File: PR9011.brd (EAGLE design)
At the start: 148 x 100 mm, 65 parts, among them J1 M3_SCREW_POST, SW1 SPST_TACT-KMR2, Y1 32.768kHz

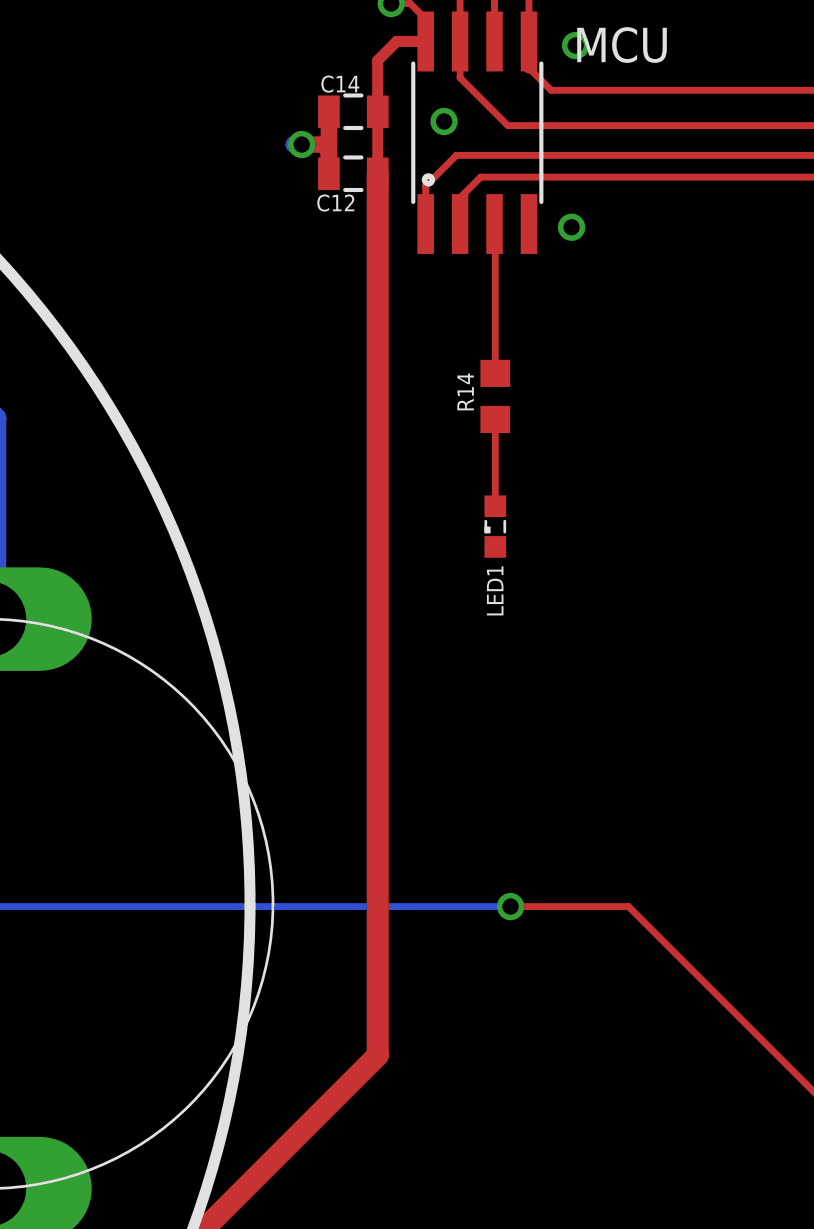
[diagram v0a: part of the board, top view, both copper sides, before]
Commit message: Updated SCH
Updated Pullup Resist & Decoupling Vals
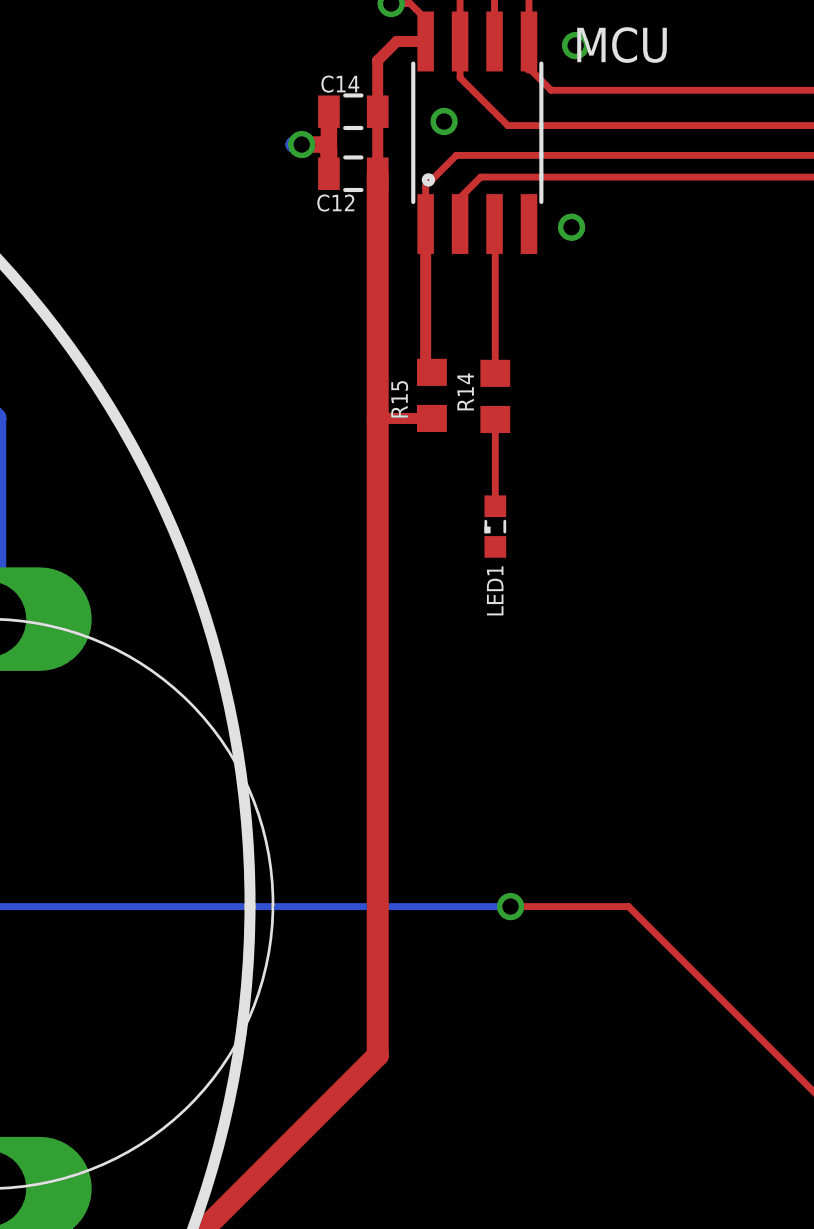
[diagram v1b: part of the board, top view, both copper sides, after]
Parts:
- added R15: 10K, resistor:R0603
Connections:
- net PB5: now also R15.2
- net VCC: now also R15.1
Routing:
- net PB5: track 23.7 -> 29.4 mm
- net VCC: track 183.8 -> 185.8 mm
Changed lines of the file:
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@@
 </element>
 <element name="VARI" library="coilcraft-trimmer" package="146/150" value="" x="34.7" y="31.85" smashed="yes" rot="R180"/>
+<element name="R15" library="resistor" package="R0603" value="10K" x="115.1" y="56.85" smashed="yes" rot="R90">
+<attribute name="NAME" x="114.211" y="55.961" size="0.6096" layer="25" rot="R90"/>
+<attribute name="VALUE" x="117.132" y="55.961" size="1.27" layer="27" rot="R90"/>
+</element>
 </elements>
 <signals>
@@
 <wire x1="99.082" y1="18.49" x2="92.452" y2="18.49" width="0.8128" layer="1"/>
 <wire x1="100.736" y1="20.144" x2="113.102" y2="32.51" width="0.8128" layer="1"/>
-<wire x1="113.102" y1="32.51" x2="113.102" y2="65.024" width="0.8128" layer="1"/>
+<wire x1="113.102" y1="32.51" x2="113.102" y2="56" width="0.8128" layer="1"/>
+<wire x1="113.102" y1="56" x2="113.102" y2="65.024" width="0.8128" layer="1"/>
 <wire x1="114.869" y1="69.9008" x2="114.8682" y2="69.9" width="0.254" layer="1"/>
 <wire x1="113.102" y1="67.31" x2="113.1" y2="67.312" width="0.4064" layer="1"/>
@@
 <wire x1="78.75" y1="14.75" x2="82.49" y2="18.49" width="0.6096" layer="1"/>
 <wire x1="82.49" y1="18.49" x2="92.452" y2="18.49" width="0.6096" layer="1"/>
+<contactref element="R15" pad="1"/>
+<wire x1="115.1" y1="56" x2="113.102" y2="56" width="0.4064" layer="1"/>
 </signal>
 <signal name="N$4">
@@
 <wire x1="116" y1="65.7" x2="134.64" y2="65.7" width="0.254" layer="1"/>
 <wire x1="134.64" y1="65.7" x2="136.078" y2="64.262" width="0.254" layer="1"/>
+<contactref element="R15" pad="2"/>
+<wire x1="115.1" y1="57.7" x2="114.869" y2="57.7" width="0.4064" layer="1"/>
+<wire x1="114.869" y1="57.7" x2="114.869" y2="63.1698" width="0.4064" layer="1"/>
 </signal>
 <signal name="PB1">

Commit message: Updated SCH
Updated SCH
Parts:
- C10: value 1.0uF -> 22nF
- C11: value 1.0uF -> 4.7uF
- C8: value 1.0uF -> .1uF
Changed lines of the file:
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@@
 <?xml version="1.0" encoding="utf-8"?>
 <!DOCTYPE eagle SYSTEM "eagle.dtd">
-<eagle version="6.6.0">
+<eagle version="7.2.0">
 <drawing>
 <settings>
@@
 <layer number="56" name="wert" color="7" fill="1" visible="no" active="no"/>
 <layer number="57" name="tCAD" color="7" fill="1" visible="no" active="no"/>
-<layer number="90" name="Modules" color="5" fill="1" visible="yes" active="yes"/>
+<layer number="90" name="Modules" color="5" fill="1" visible="no" active="no"/>
 <layer number="91" name="Nets" color="2" fill="1" visible="no" active="no"/>
 <layer number="92" name="Busses" color="1" fill="1" visible="no" active="no"/>
@@
 <pass name="Default">
 <param name="RoutingGrid" value="50mil"/>
+<param name="AutoGrid" value="1"/>
+<param name="Efforts" value="0"/>
+<param name="TopRouterVariant" value="1"/>
 <param name="tpViaShape" value="round"/>
 <param name="PrefDir.1" value="|"/>
@@
 <attribute name="VALUE" x="33.919" y="38.876" size="0.4064" layer="27" rot="R270"/>
 </element>
-<element name="C8" library="SparkFun-Capacitors" package="0805" value="1.0uF" x="21.136" y="42.21" smashed="yes" rot="R180">
+<element name="C8" library="SparkFun-Capacitors" package="0805" value=".1uF" x="21.136" y="42.21" smashed="yes" rot="R180">
 <attribute name="PROD_ID" value="CAP-11625" x="5.896" y="123.49" size="1.778" layer="27" rot="R180" display="off"/>
 <attribute name="NAME" x="17.2845" y="42.452" size="0.6096" layer="25" rot="R180"/>
 <attribute name="VALUE" x="22.152" y="43.607" size="0.4064" layer="27" rot="R180"/>
 </element>
-<element name="C10" library="SparkFun-Capacitors" package="0805" value="1.0uF" x="20.986" y="31.768" smashed="yes" rot="R180">
+<element name="C10" library="SparkFun-Capacitors" package="0805" value="22nF" x="20.986" y="31.768" smashed="yes" rot="R180">
 <attribute name="PROD_ID" value="CAP-11625" x="-36.164" y="109.238" size="1.778" layer="27" rot="R180" display="off"/>
 <attribute name="NAME" x="17.6925" y="31.802" size="0.6096" layer="25" rot="R180"/>
 <attribute name="VALUE" x="22.002" y="33.165" size="0.4064" layer="27" rot="R180"/>
 </element>
-<element name="C11" library="SparkFun-Capacitors" package="0805" value="1.0uF" x="20.986" y="29.544" smashed="yes" rot="R180">
+<element name="C11" library="SparkFun-Capacitors" package="0805" value="4.7uF" x="20.986" y="29.544" smashed="yes" rot="R180">
 <attribute name="PROD_ID" value="CAP-11625" x="-39.974" y="107.014" size="1.778" layer="27" rot="R180" display="off"/>
 <attribute name="NAME" x="17.5685" y="29.752" size="0.6096" layer="25" rot="R180"/>

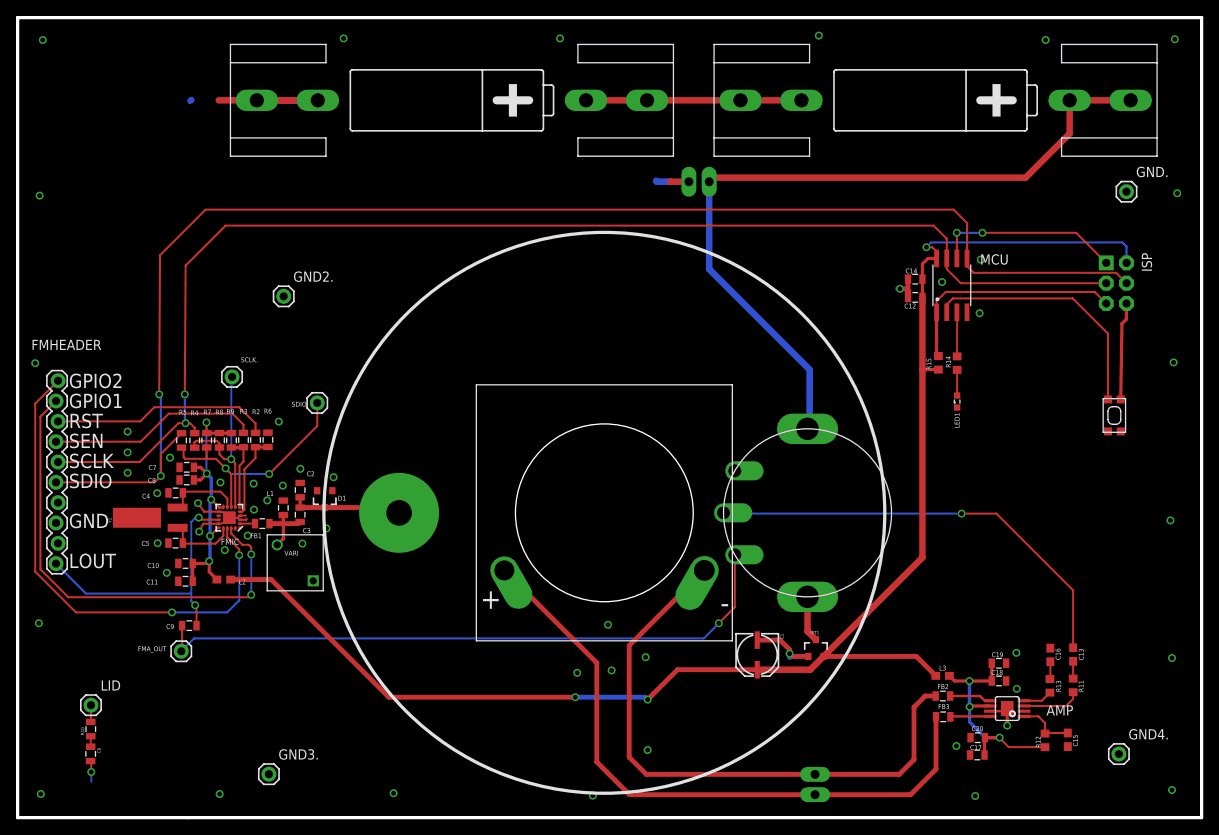
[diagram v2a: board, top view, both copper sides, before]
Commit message: Updated SCH
Updated SCH
JST
Fiducials
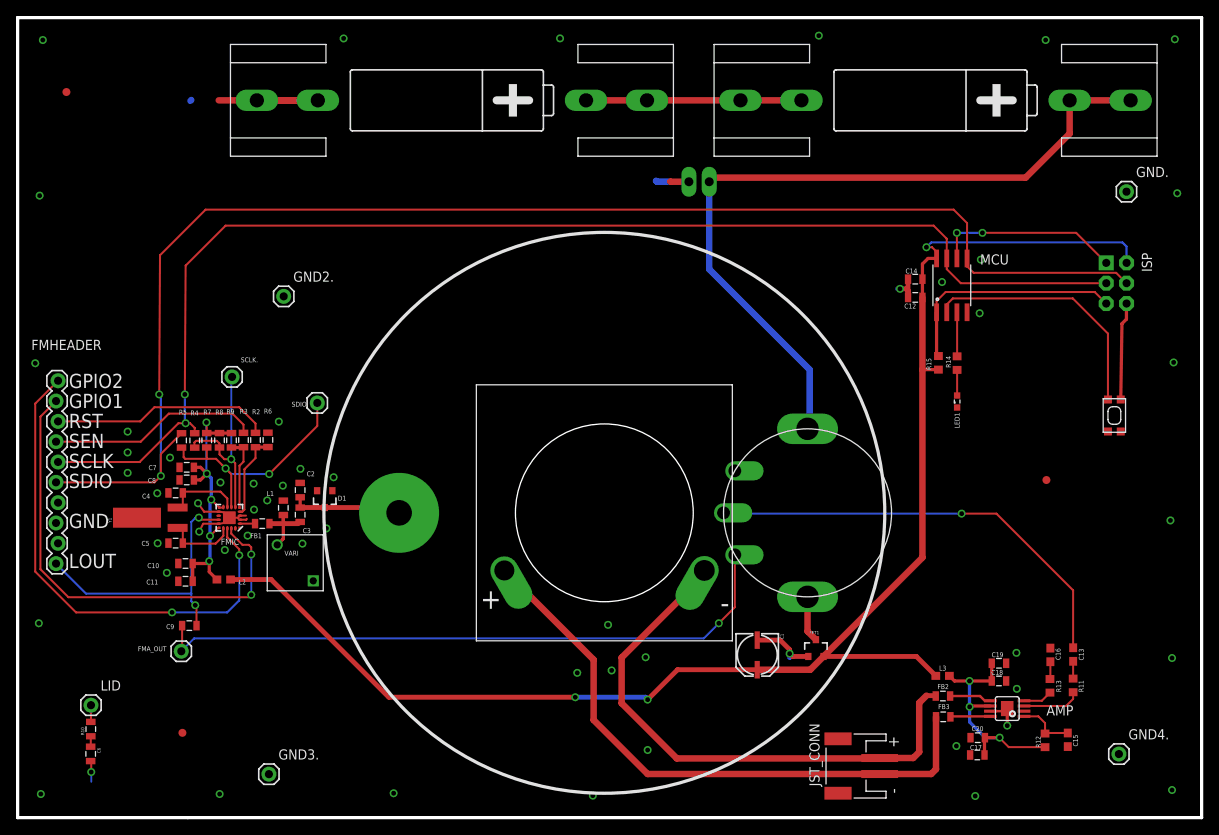
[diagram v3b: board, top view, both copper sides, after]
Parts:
- removed SPK: M02PTH3, SparkFun-Connectors:1X02_LONGPADS
- added JST_CONN: (no value), adafruit:JST-PH-2-SMT-RA
- added U$1, U$2, U$4: FIDUCIAL, adafruit:FIDUCIAL_1MM
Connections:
- net N$9: now also JST_CONN.1; no longer SPK.1
- net OUT-: now also JST_CONN.2; no longer SPK.2
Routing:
- net OUT-: track 80.7 -> 75.7 mm
- net N$9: track 74.3 -> 70.4 mm
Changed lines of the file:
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@@
 <?xml version="1.0" encoding="utf-8"?>
 <!DOCTYPE eagle SYSTEM "eagle.dtd">
-<eagle version="7.2.0">
+<eagle version="6.6.0">
 <drawing>
 <settings>
@@
 <setting verticaltext="up"/>
 </settings>
-<grid distance="0.05" unitdist="mm" unit="mm" style="lines" multiple="1" display="yes" altdistance="0.025" altunitdist="inch" altunit="inch"/>
+<grid distance="0.1" unitdist="mm" unit="mm" style="lines" multiple="1" display="yes" altdistance="0.025" altunitdist="inch" altunit="inch"/>
 <layers>
 <layer number="1" name="Top" color="4" fill="1" visible="yes" active="yes"/>
@@
 <pass name="Default">
 <param name="RoutingGrid" value="50mil"/>
-<param name="AutoGrid" value="1"/>
-<param name="Efforts" value="0"/>
-<param name="TopRouterVariant" value="1"/>
 <param name="tpViaShape" value="round"/>
 <param name="PrefDir.1" value="|"/>
@@
 </element>
 <element name="SW1" library="adafruit" package="KMR2" value="SPST_TACT-KMR2" x="137.092" y="50.266" smashed="yes" rot="R90"/>
-<element name="SPK" library="SparkFun-Connectors" package="1X02_LONGPADS" value="M02PTH3" x="99.684" y="5.408" rot="R270"/>
 <element name="ISP" library="SparkFun-Connectors" package="2X3-NS" value="AVR_SPI_PRG_6NS" x="137.348" y="66.802" locked="yes" smashed="yes" rot="R270">
 <attribute name="NAME" x="140.523" y="70.612" size="1.27" layer="25" ratio="10" rot="R270"/>
@@
 <attribute name="VALUE" x="117.132" y="55.961" size="1.27" layer="27" rot="R90"/>
 </element>
+<element name="JST_CONN" library="adafruit" package="JST-PH-2-SMT-RA" value="" x="104.05" y="6.45" rot="R90"/>
+<element name="U$1" library="adafruit" package="FIDUCIAL_1MM" value="FIDUCIAL" x="128.6" y="42.2"/>
+<element name="U$2" library="adafruit" package="FIDUCIAL_1MM" value="FIDUCIAL" x="6.1" y="90.7"/>
+<element name="U$4" library="adafruit" package="FIDUCIAL_1MM" value="FIDUCIAL" x="20.6" y="10.6"/>
 </elements>
 <signals>
@@
 </signal>
 <signal name="OUT-">
-<contactref element="SPK" pad="2"/>
 <contactref element="U$3" pad="+"/>
 <contactref element="FB3" pad="1"/>
-<wire x1="114.8" y1="12.6" x2="114.8" y2="6.05" width="0.6096" layer="1"/>
-<wire x1="114.8" y1="6.05" x2="111.618" y2="2.868" width="0.6096" layer="1"/>
-<wire x1="111.618" y1="2.868" x2="99.684" y2="2.868" width="0.6096" layer="1"/>
-<wire x1="99.684" y1="2.868" x2="76.482" y2="2.868" width="0.6096" layer="1"/>
-<wire x1="76.482" y1="2.868" x2="72.4" y2="6.95" width="0.6096" layer="1"/>
-<wire x1="72.4" y1="6.95" x2="72.4" y2="19.34" width="0.6096" layer="1"/>
-<wire x1="72.4" y1="19.34" x2="60.84" y2="30.9" width="0.6096" layer="1"/>
+<wire x1="114.8" y1="12.6" x2="114.8" y2="6.05" width="0.8128" layer="1"/>
+<contactref element="JST_CONN" pad="2"/>
+<wire x1="114.8" y1="6.05" x2="114.2" y2="5.45" width="0.8128" layer="1"/>
+<wire x1="114.2" y1="5.45" x2="107.75" y2="5.45" width="0.8128" layer="1"/>
+<wire x1="107.75" y1="5.45" x2="78.75" y2="5.45" width="0.8128" layer="1"/>
+<wire x1="78.75" y1="5.45" x2="72" y2="12.2" width="0.8128" layer="1"/>
+<wire x1="72" y1="12.2" x2="72" y2="19.74" width="0.8128" layer="1"/>
+<wire x1="72" y1="19.74" x2="60.84" y2="30.9" width="0.8128" layer="1"/>
 </signal>
 <signal name="N$34">
@@
 </signal>
 <signal name="N$9">
-<contactref element="SPK" pad="1"/>
+<contactref element="U$3" pad="-"/>
 <contactref element="FB2" pad="2"/>
-<contactref element="U$3" pad="-"/>
-<wire x1="114.764" y1="15.2" x2="113.45" y2="15.2" width="0.6096" layer="1"/>
-<wire x1="113.45" y1="15.2" x2="112.05" y2="13.8" width="0.6096" layer="1"/>
-<wire x1="112.05" y1="13.8" x2="112.05" y2="7.25" width="0.6096" layer="1"/>
-<wire x1="112.05" y1="7.25" x2="110.208" y2="5.408" width="0.6096" layer="1"/>
-<wire x1="110.208" y1="5.408" x2="99.684" y2="5.408" width="0.6096" layer="1"/>
-<wire x1="99.684" y1="5.408" x2="78.592" y2="5.408" width="0.6096" layer="1"/>
-<wire x1="78.592" y1="5.408" x2="76.45" y2="7.55" width="0.6096" layer="1"/>
-<wire x1="76.45" y1="7.55" x2="76.45" y2="21.51" width="0.6096" layer="1"/>
-<wire x1="76.45" y1="21.51" x2="85.84" y2="30.9" width="0.6096" layer="1"/>
+<contactref element="JST_CONN" pad="1"/>
+<wire x1="107.75" y1="7.45" x2="108.3" y2="7.45" width="0.6096" layer="1"/>
+<wire x1="108.3" y1="7.45" x2="111.95" y2="7.45" width="0.8128" layer="1"/>
+<wire x1="111.95" y1="7.45" x2="112.7" y2="8.2" width="0.8128" layer="1"/>
+<wire x1="112.7" y1="8.2" x2="112.7" y2="14.35" width="0.8128" layer="1"/>
+<wire x1="112.7" y1="14.35" x2="113.6" y2="15.25" width="0.8128" layer="1"/>
+<wire x1="113.6" y1="15.25" x2="114.714" y2="15.25" width="0.6096" layer="1"/>
+<wire x1="114.714" y1="15.25" x2="114.764" y2="15.2" width="0.6096" layer="1"/>
+<wire x1="85.84" y1="30.9" x2="85.84" y2="30.34" width="0.8128" layer="1"/>
+<wire x1="85.84" y1="30.34" x2="75.5" y2="20" width="0.8128" layer="1"/>
+<wire x1="75.5" y1="20" x2="75.5" y2="14.3" width="0.8128" layer="1"/>
+<wire x1="75.5" y1="14.3" x2="82.4" y2="7.4" width="0.8128" layer="1"/>
+<wire x1="82.4" y1="7.4" x2="108.25" y2="7.4" width="0.8128" layer="1"/>
+<wire x1="108.25" y1="7.4" x2="108.3" y2="7.45" width="0.6096" layer="1"/>
 </signal>
 </signals>
